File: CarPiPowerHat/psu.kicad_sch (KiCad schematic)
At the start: 46 parts, among them IC1 AP2331TDSA-7, IC2 BD2226G-TR, J7 USB_A, J8 Conn_01x02_Male, Q1 DMMT5401, Q2 DMG2305, Q4 DMP3013SFV-7, U3 AP64501SP-13

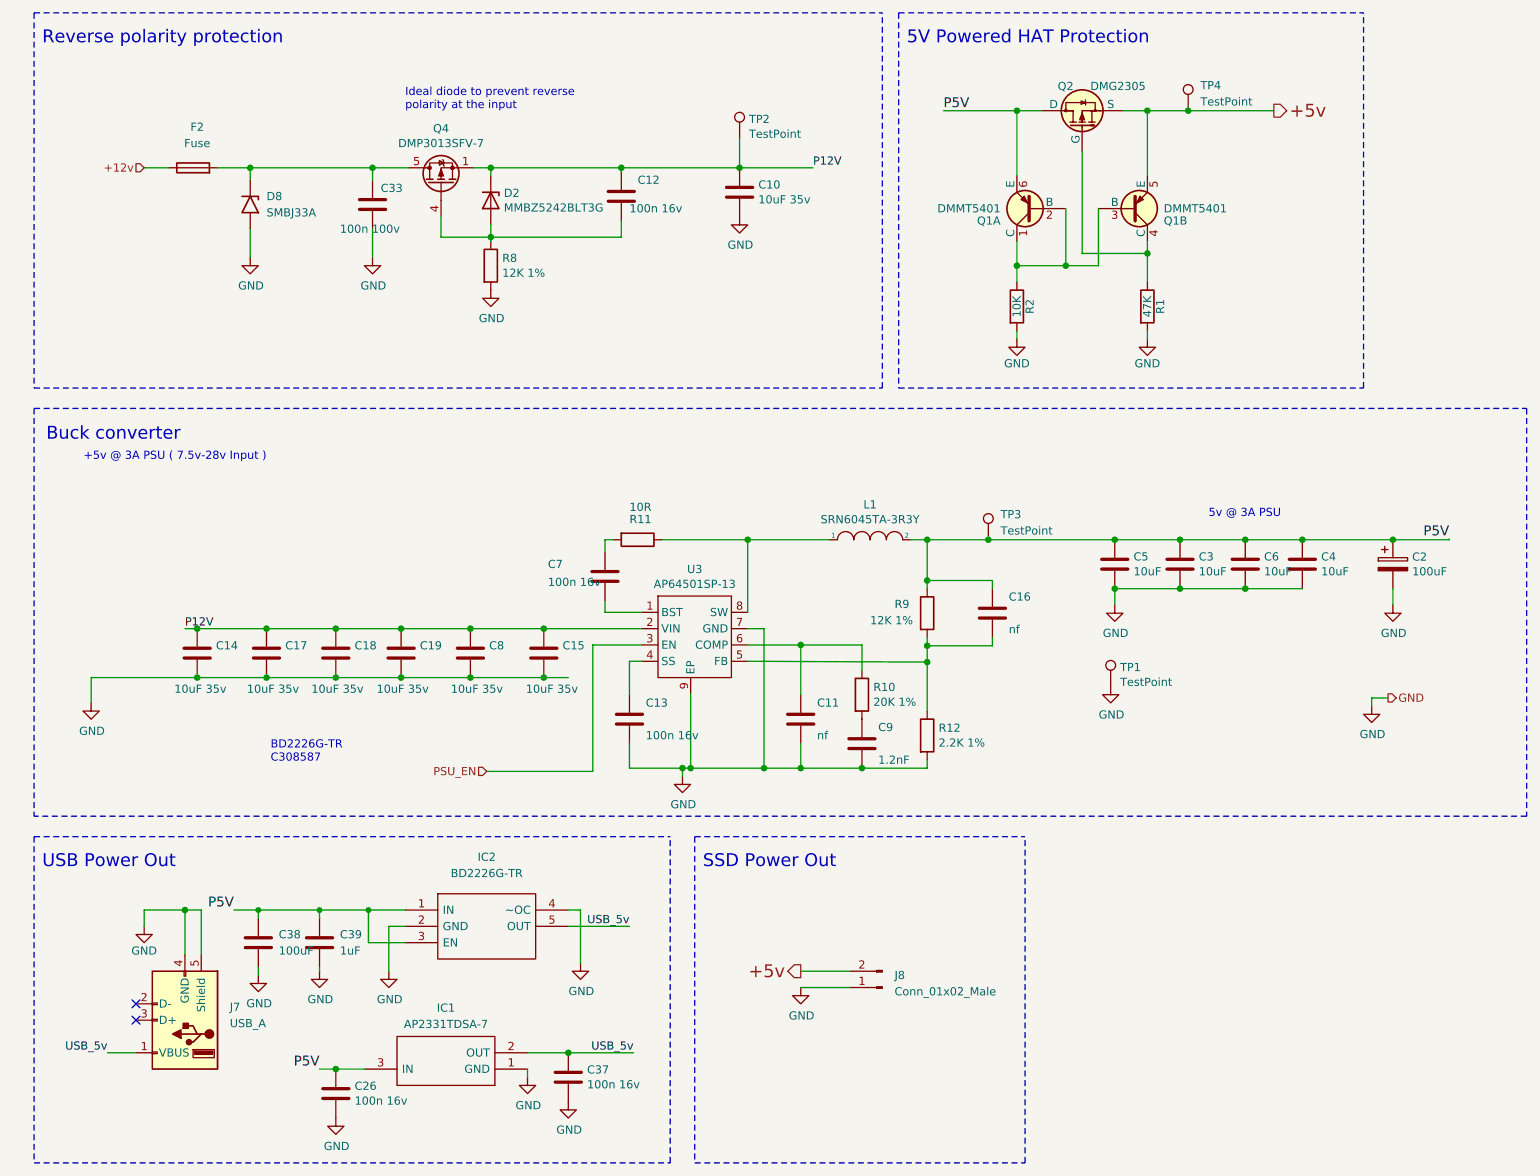
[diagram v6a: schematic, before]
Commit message: removed unnecessary reverse polarity protection
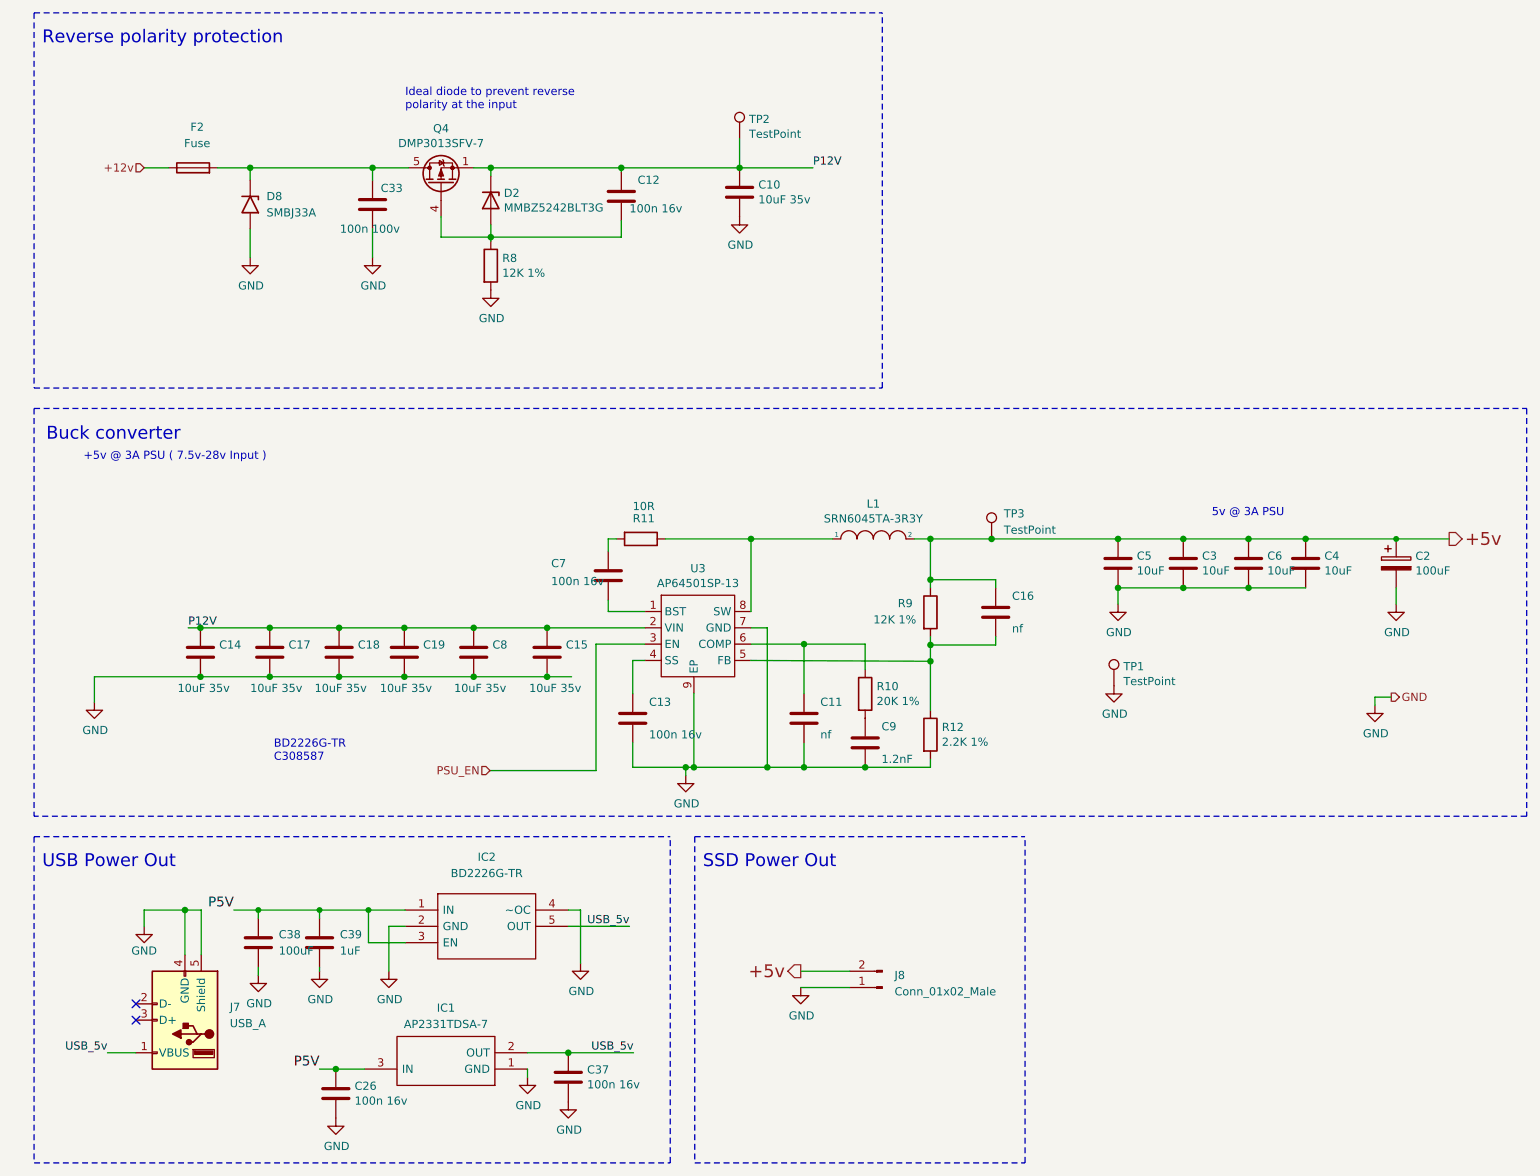
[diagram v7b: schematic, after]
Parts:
- removed Q1: DMMT5401, project_footprints:SOT26, symbol CarPiPowerHat:DMMT5401
- removed Q2: DMG2305, Package_TO_SOT_SMD:SOT-23, symbol CarPiPowerHat:DMG2305UX
- removed R1: 47K, Resistor_SMD:R_0603_1608Metric, symbol Device:R
- removed R2: 10K, Resistor_SMD:R_0603_1608Metric, symbol Device:R
- removed TP4: TestPoint, TestPoint:TestPoint_Pad_2.0x2.0mm, symbol Connector:TestPoint
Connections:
- net +5v: now also C16.1, C2.1, C3.1, C4.1, C5.1, C6.1, L1.2, R9.1, TP3.1
- net P5V: no longer C16.1, C2.1, C3.1, C4.1, C5.1, C6.1, L1.2, R9.1, TP3.1
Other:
- note removed: "5V Powered HAT Protection"
- moved on the sheet: C11, C13, C14, C15, C16, C17, C18, C19, C2, C3, C4, C5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

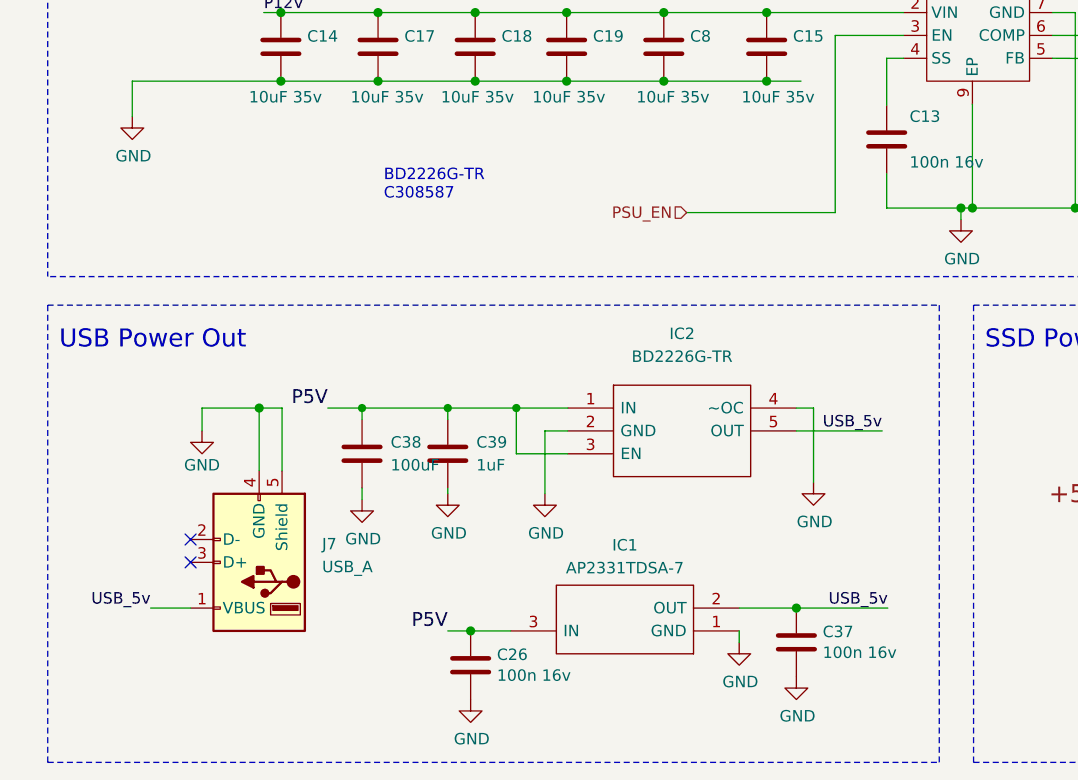
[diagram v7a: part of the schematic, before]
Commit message: Some rerouting
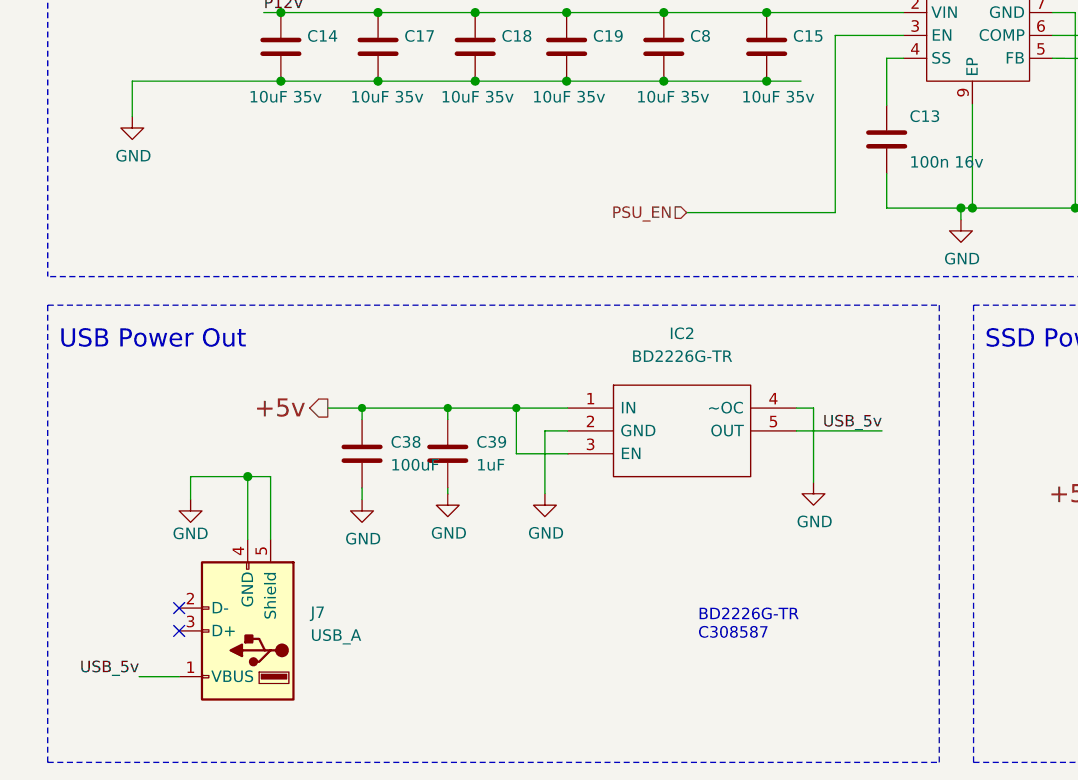
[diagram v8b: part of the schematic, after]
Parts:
- removed C26, C37: 100n 16v, Capacitor_SMD:C_0402_1005Metric, symbol Device:C
- removed IC1: AP2331TDSA-7, ap2331:SOT96P240X110-3N, symbol AP2331TDSA-7:AP2331TDSA-7
- IC2: footprint SOT95P280X125-5N -> SamacSys_Parts:SOT95P280X125-5N
- TP1, TP2, TP3: footprint TestPoint:TestPoint_Pad_2.0x2.0mm -> TestPoint:TestPoint_Pad_D1.0mm
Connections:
- net P5V is gone; now on net +5v: C38.1, C39.1, IC2.1 (IN), IC2.3 (EN)
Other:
- moved on the sheet: J7
